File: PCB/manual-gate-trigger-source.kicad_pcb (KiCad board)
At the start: 2 copper layers, 108.9 x 110.5 mm, 115 parts, among them J1 PWR, J10 IN1, J11 Conn_01x04, J12 Conn_01x04, J2 OUTa, J3 OUTb, J4 OUTa, J5 OUTb, J6 OUTa, J7 OUTb, J8 OUTa, J9 OUTb, Q2 BC547, Q3 BC547, Q4 BC547, Q5 BC547, Q6 BC547, SW2 ON/ON, SW3 ON/ON, SW4 ON/ON, SW5 ON/ON, SW6 SW_Push, SW7 SW_Push, SW8 SW_Push, U2 LM555xN, U3 LM555xN, U4 LM555xN, U5 LM555xN, U6 LM317L_TO92

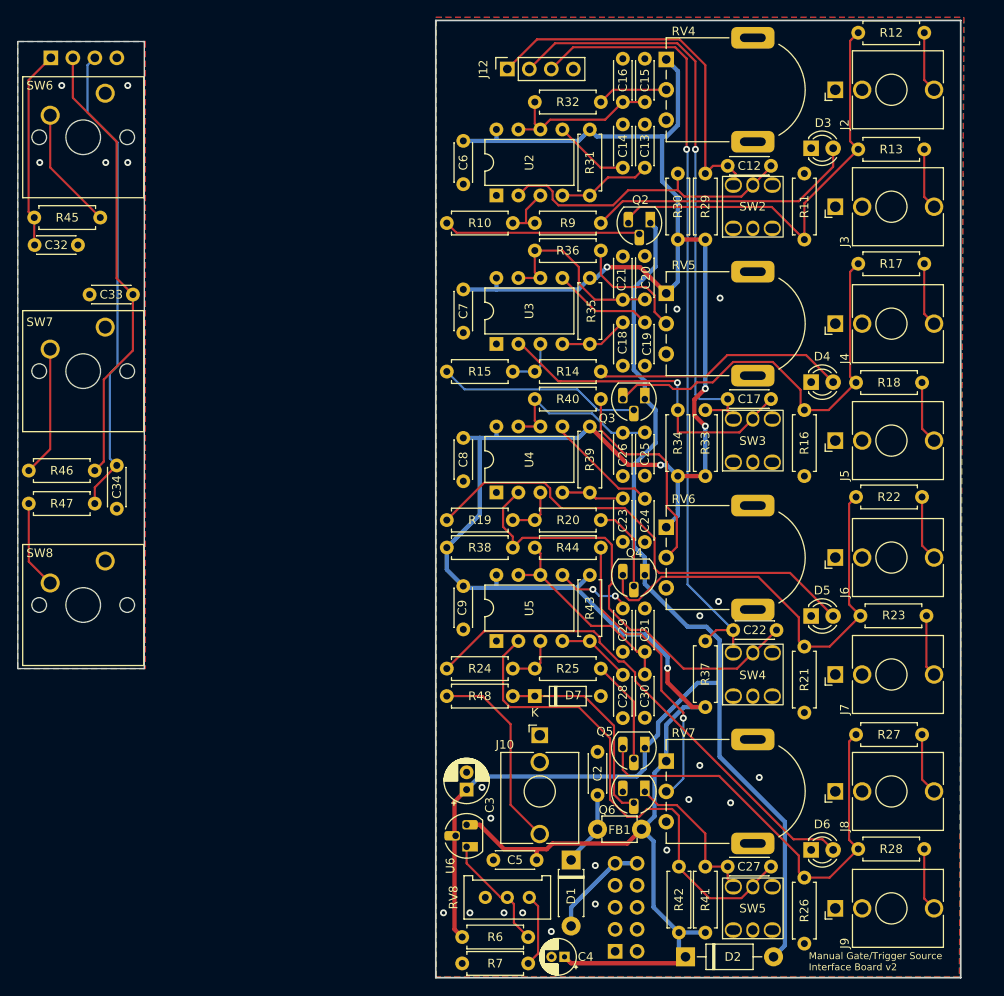
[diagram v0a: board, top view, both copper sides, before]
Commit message: :memo: Geographically reannotate the PCB
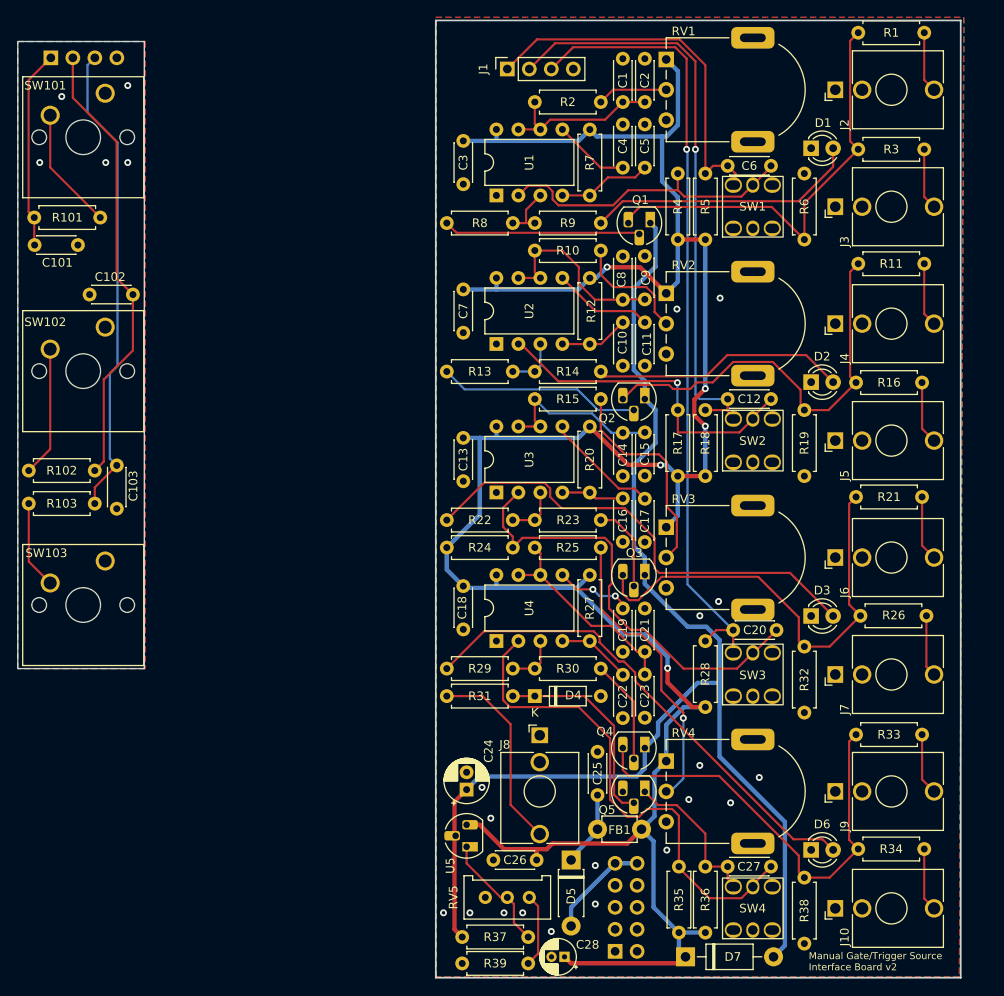
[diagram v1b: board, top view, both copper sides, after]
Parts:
- renumbered C16 to C1, C18 to C10, C32 to C101, C33 to C102, C34 to C103, C19 to C11, C17 to C12, C8 to C13, C26 to C14, C25 to C15, C23 to C16, C24 to C17, C9 to C18, C29 to C19, C15 to C2, C22 to C20, C31 to C21, C28 to C22, C30 to C23, C3 to C24, C2 to C25, C5 to C26, C4 to C28, C6 to C3, C14 to C4, C13 to C5, C12 to C6, C21 to C8, C20 to C9, D3 to D1, D4 to D2, D5 to D3, D7 to D4, D1 to D5, D2 to D7, J12 to J1, J9 to J10, J11 to J101, J1 to J11, J10 to J8, J8 to J9, Q2 to Q1, Q3 to Q2, Q4 to Q3, Q5 to Q4, Q6 to Q5, R12 to R1, R36 to R10, R45 to R101, R46 to R102, R47 to R103, R17 to R11, R35 to R12, R15 to R13, R40 to R15, R18 to R16, R34 to R17, R33 to R18, R16 to R19, R32 to R2, R39 to R20, R22 to R21, R19 to R22, R20 to R23, R38 to R24, R44 to R25, R23 to R26, R43 to R27, R37 to R28, R24 to R29, R13 to R3, R25 to R30, R48 to R31, R21 to R32, R27 to R33, R28 to R34, R42 to R35, R41 to R36, R6 to R37, R26 to R38, R7 to R39, R30 to R4, R29 to R5, R11 to R6, R31 to R7, R10 to R8, RV4 to RV1, RV5 to RV2, RV6 to RV3, RV7 to RV4, RV8 to RV5, SW2 to SW1, SW6 to SW101, SW7 to SW102, SW8 to SW103, SW3 to SW2, SW4 to SW3, SW5 to SW4, U2 to U1, U3 to U2, U4 to U3, U5 to U4, U6 to U5
